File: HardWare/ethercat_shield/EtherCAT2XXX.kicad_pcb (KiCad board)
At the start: 2 copper layers, 144 parts, among them CN1 5019530507, CN2 5019530507, J2 Conn_01x03, J3 Conn_01x04, J4 Conn_01x02, J5 Conn_01x02, J6 Conn_01x03, J7 Conn_01x04, J8 USB_C_Receptacle_USB2.0, SW1 SW_Push, U2 RT8075, U3 SRV05-4, U4 SRV05-4, U5 STM32F407VETx, U6 TJA1051T-3, U7 TJA1051T-3, U8 AX58100-LQPF80, U9 BL24C16F-PARC, X1 25M, Y1 8M, Y2 32.768KHz

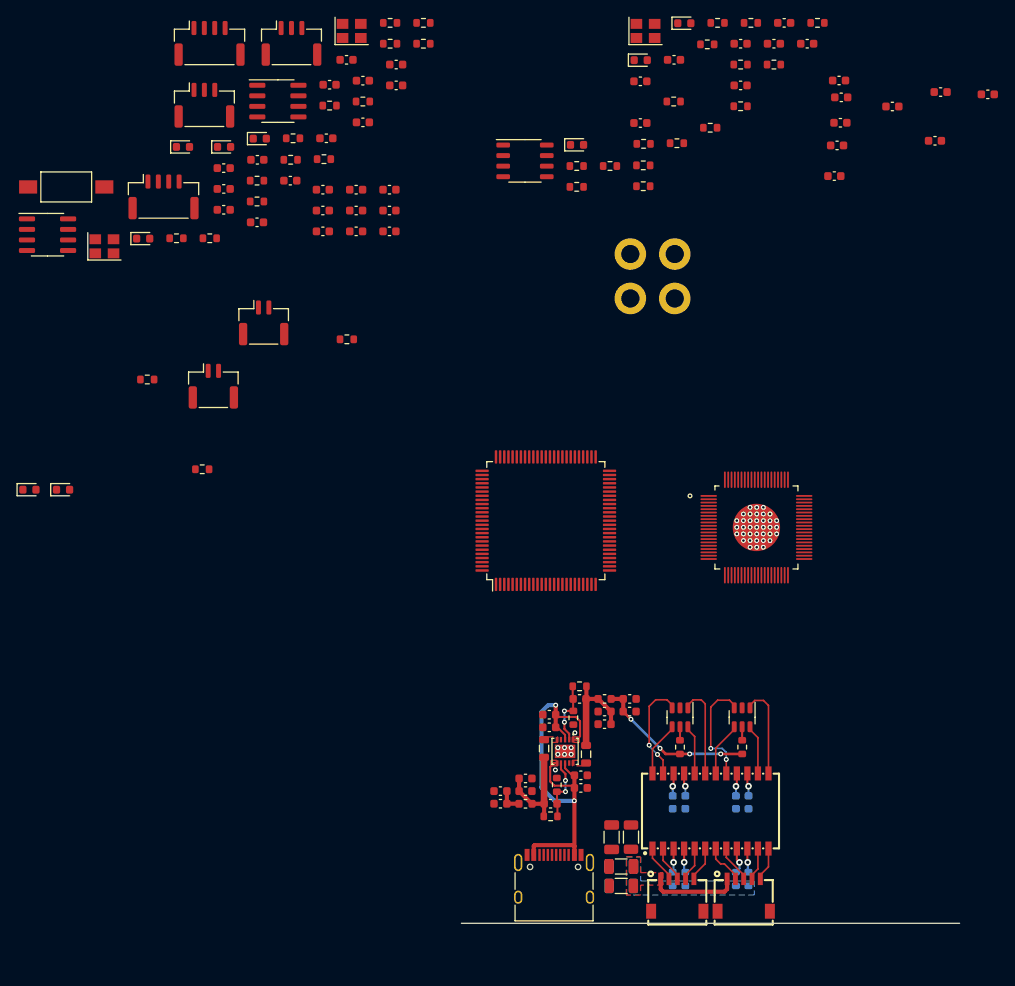
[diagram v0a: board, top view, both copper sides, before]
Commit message: 'ethercat_shield' PCB_layout completed
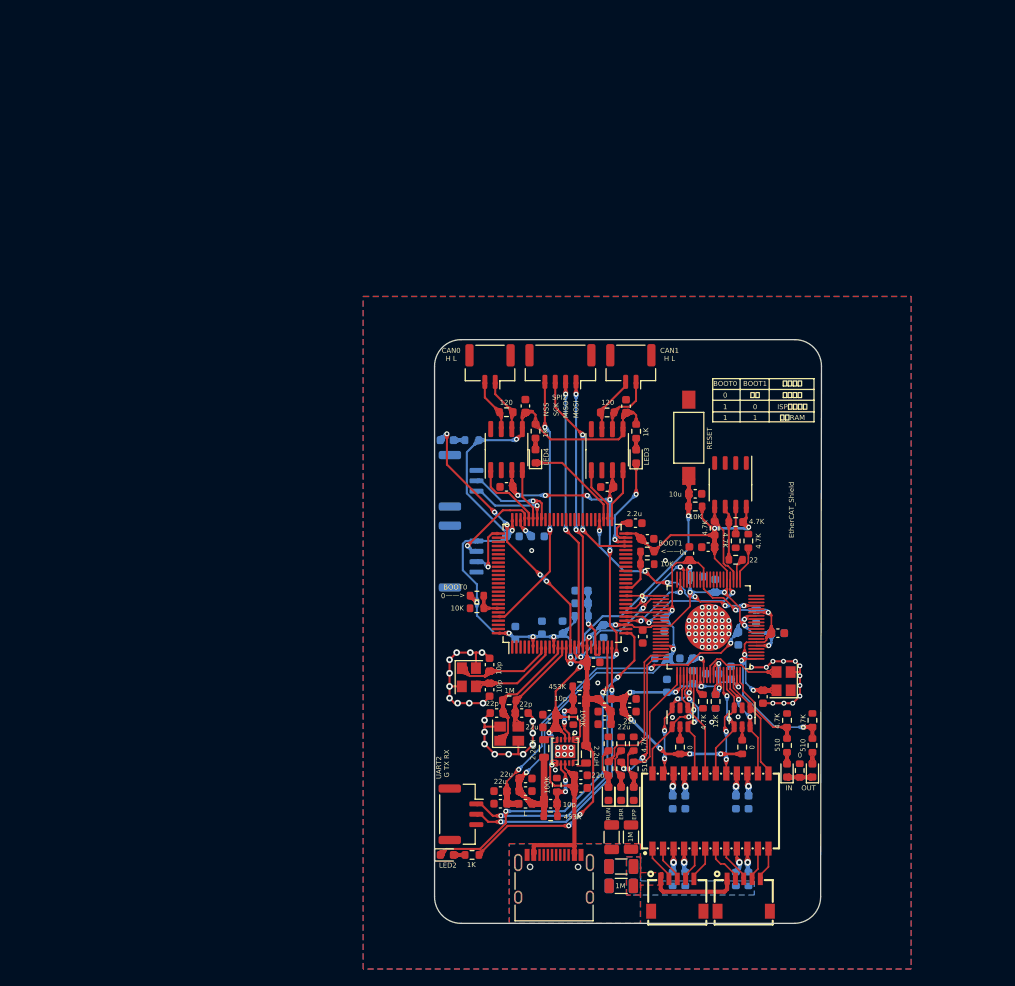
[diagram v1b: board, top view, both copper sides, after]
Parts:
- removed C59, C61: 100n, Capacitor_SMD:C_0603_1608Metric
- removed H1, H2, H3, H4: MountingHole, MountingHole:MountingHole_2.2mm_M2_DIN965_Pad
- C35, C38, C44, C46: value 100nF -> 100n
- C36, C37, C39, C40, C41, C42, C43, C45, C47, C48, C49: value 100nF -> 100n; moved to B.Cu
- C51, C52, C53, C57, C58, C60, C62, C64, C65, D3, J2, J3, R22, R30, R45: moved to B.Cu
- moved D2 100.2 mm to (129.1, 110.1), turned to 90 degrees
- moved D1 93.5 mm to (126.0, 110.1), turned to 90 degrees
- moved D8 93.1 mm to (106.1, 112.9), turned to 90 degrees
- moved R23 91.7 mm to (88.1, 120.3)
- moved R19 91.6 mm to (127.6, 110.1), turned to 90 degrees
- moved R37 91.2 mm to (106.1, 109.9), turned to 90 degrees
- moved J6 90.8 mm to (86.8, 115.4), turned to -90 degrees
- moved D9 88.4 mm to (107.6, 112.9), turned to 90 degrees
- moved Y1 86.7 mm to (92.6, 105.7)
- moved R36 86.3 mm to (104.5, 109.9), turned to 90 degrees
- moved R39 84.4 mm to (126.0, 104.0), turned to 90 degrees
- moved D4 82.8 mm to (85.1, 120.3)
- moved SW1 80.8 mm to (114.2, 70.0), turned to -90 degrees
- moved R18 80.7 mm to (129.1, 107.1), turned to -90 degrees
- moved X1 80.1 mm to (125.6, 99.3), turned to 90 degrees
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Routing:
- net 3V3: track 12.3 -> 193.3 mm, vias 0 -> 18
- net 1V2: track 12.3 -> 93.2 mm, vias 0 -> 8
- net GND: track 0.00 -> 53.2 mm, vias 45 -> 83
- net A1V2: track 2.98 -> 44.8 mm, vias 0 -> 4
- net /MCU/LED2: track 0.00 -> 39.9 mm, vias 0 -> 2
- net /MCU/USART2_RX: track 0.00 -> 37.7 mm, vias 0 -> 2
- net +5V: track 50.4 -> 88.1 mm, vias 2 -> 9
- net /MCU/USART2_TX: track 0.00 -> 34.5 mm, vias 0 -> 2
- net /MCU/LED1: track 0.00 -> 33.0 mm, vias 0 -> 5
- net /MCU/SPI2_MISO: track 0.00 -> 32.6 mm, vias 0 -> 2
- net /MCU/SPI2_MOSI: track 0.00 -> 32.3 mm, vias 0 -> 2
- net /MCU/RSET: track 0.00 -> 32.1 mm, vias 0 -> 2
- net /MCU/SPI2_NSS: track 0.00 -> 31.5 mm, vias 0 -> 2
- net /ESC/RSTN: track 0.00 -> 25.3 mm, vias 0 -> 6
- net /MCU/SPI2_SCK: track 0.00 -> 25.2 mm, vias 0 -> 2
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- added copper zone on B.Cu, net Earth
- added copper zone on F.Cu, net Earth
- added copper zone on B.Cu, net GND
- added copper zone on F.Cu, net GND
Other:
- board outline added: 46.6 x 70.3 mm
- board text added: "0"
- board text added: "1"
- board text added: "10"
- board text added: "100K"
- board text added: "10K"
- board text added: "10p"
- board text added: "10u"
- board text added: "120"
- board text added: "12K"
- board text added: "1K"
- board text added: "1M"
- board text added: "2.2u"
- board text added: "2.2uH"
- board text added: "22"
- board text added: "22p"
- board text added: "22u"
- board text added: "3V3 DIO CLK G"
- board text added: "4.7K"
- board text added: "453K"
- board text added: "510"
- board text added: "75"
- board text added: "BOOT0"
- board text added: "BOOT0 ——>"
- board text added: "BOOT1"
- board text added: "BOOT1 <——"
- board text added: "CAN0 H L"
- board text added: "CAN1 H L"
- board text added: "EPP"
- board text added: "ERR"
- board text added: "EtherCAT_Shield"
- board text added: "G TX RX"
- board text added: "IN OUT"
- board text added: "ISP下载模式"
- board text added: "L"
- board text added: "LED1"
- board text added: "LED2"
- board text added: "LED3"
- board text added: "LED4"
- board text added: "MISO"
- board text added: "MOSI"
- board text added: "NSS"
- board text added: "RESET"
- board text added: "RUN"
- board text added: "SCK"
- board text added: "SPI2"
- board text added: "UART1"
- board text added: "UART2"
- board text added: "内部RAM"
- board text added: "无关"
- board text added: "用户模式"
- board text added: "用户闪存"

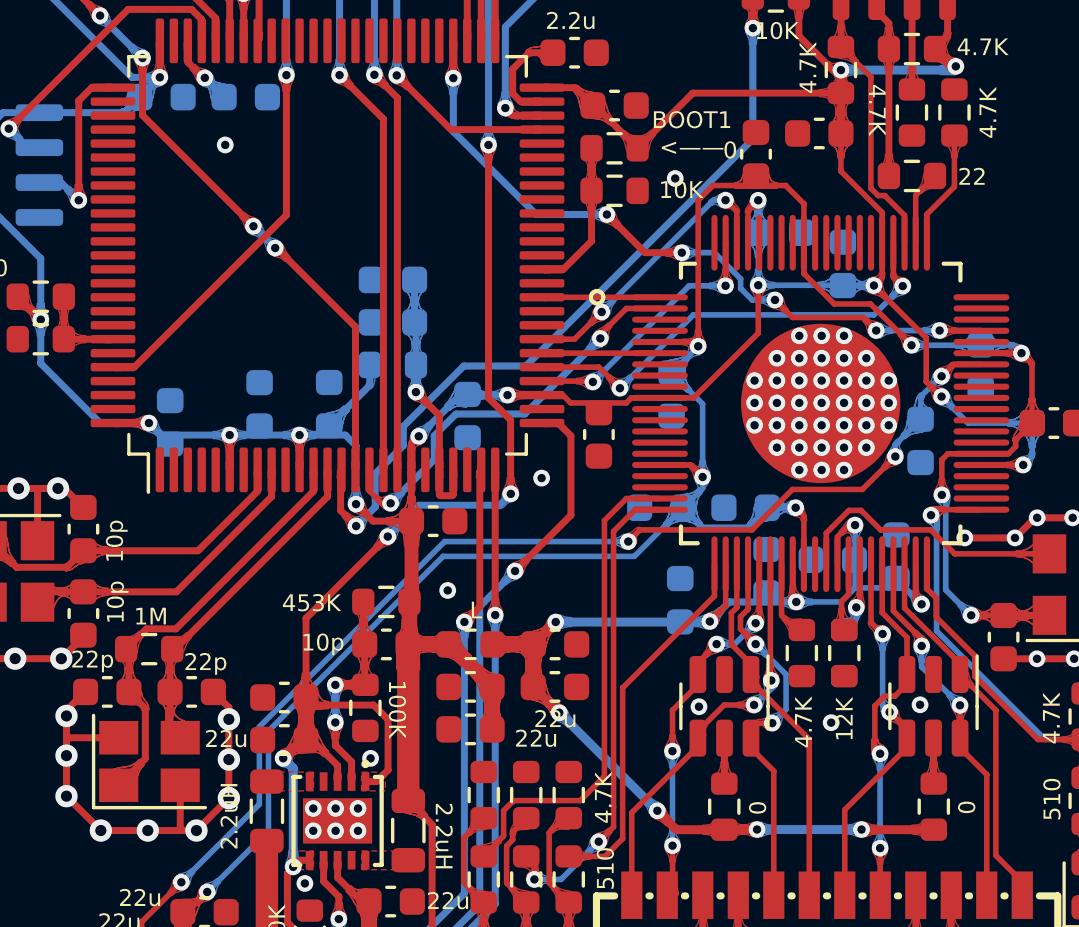
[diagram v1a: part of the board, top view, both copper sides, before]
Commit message: Adaption for Kicad 7.0
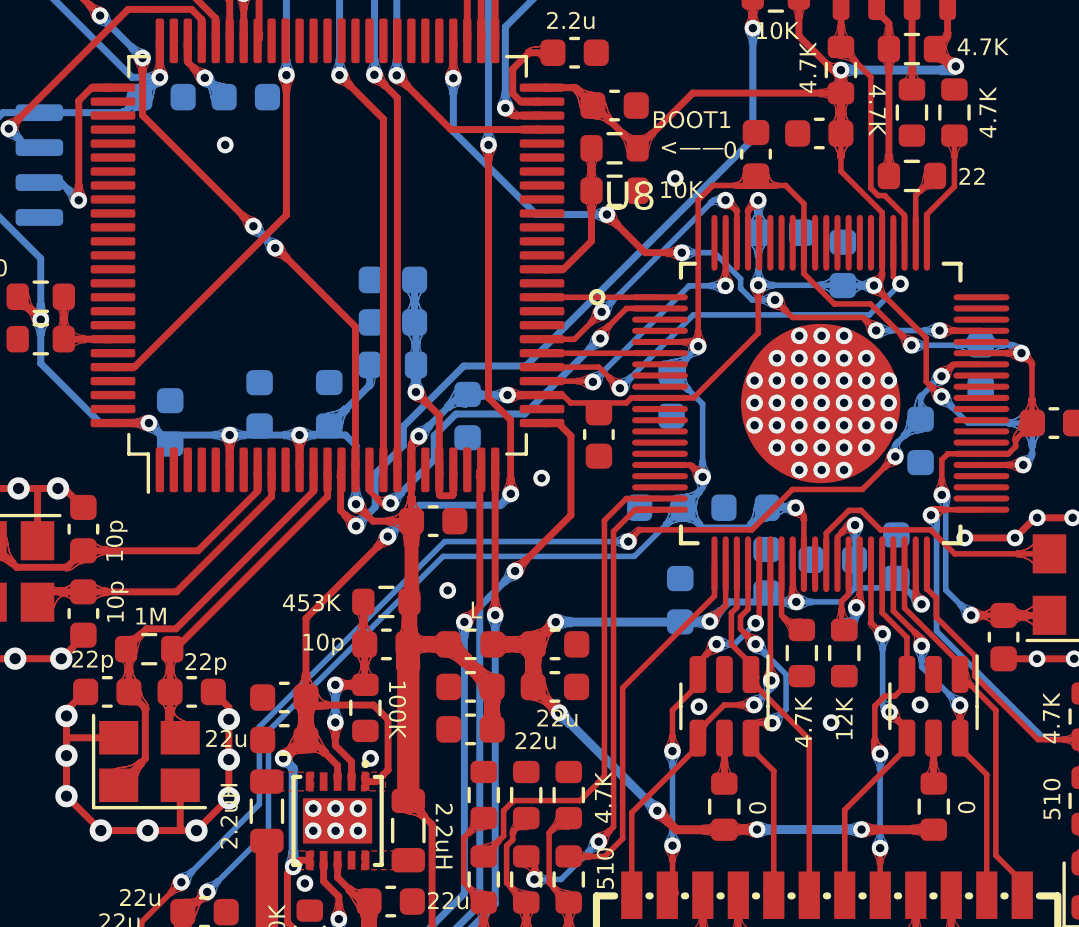
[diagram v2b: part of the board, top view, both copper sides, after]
